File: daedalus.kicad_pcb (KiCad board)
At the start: 4 copper layers, 42 x 50.2 mm, 100 parts, among them J1 CAN Bus, J2 CAN Bus, J5 A Terminal, J6 B Terminal, J7 C Terminal, J9 USB_B_Micro, Q1 AO3401A, U1 XT30, U10 TPH, U11 TPH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

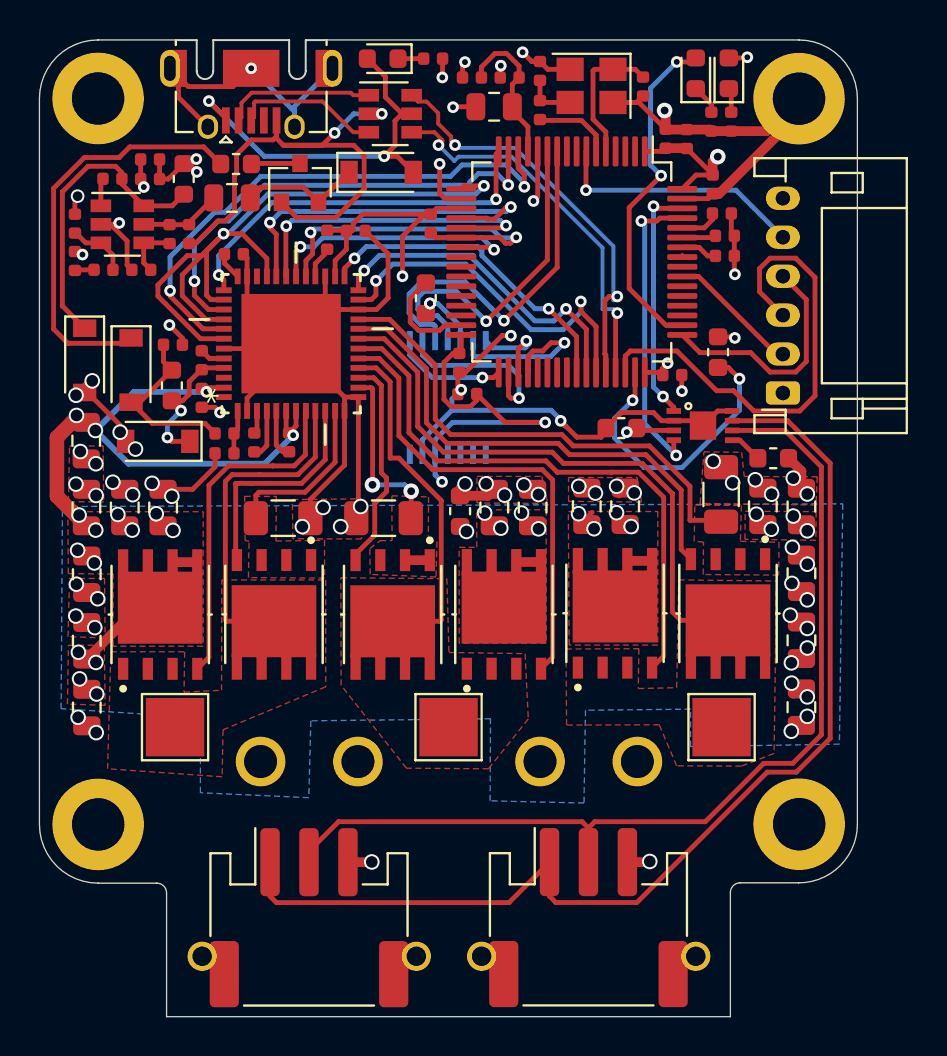
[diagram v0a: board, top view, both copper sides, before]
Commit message: Fixed design rules, fixed pours
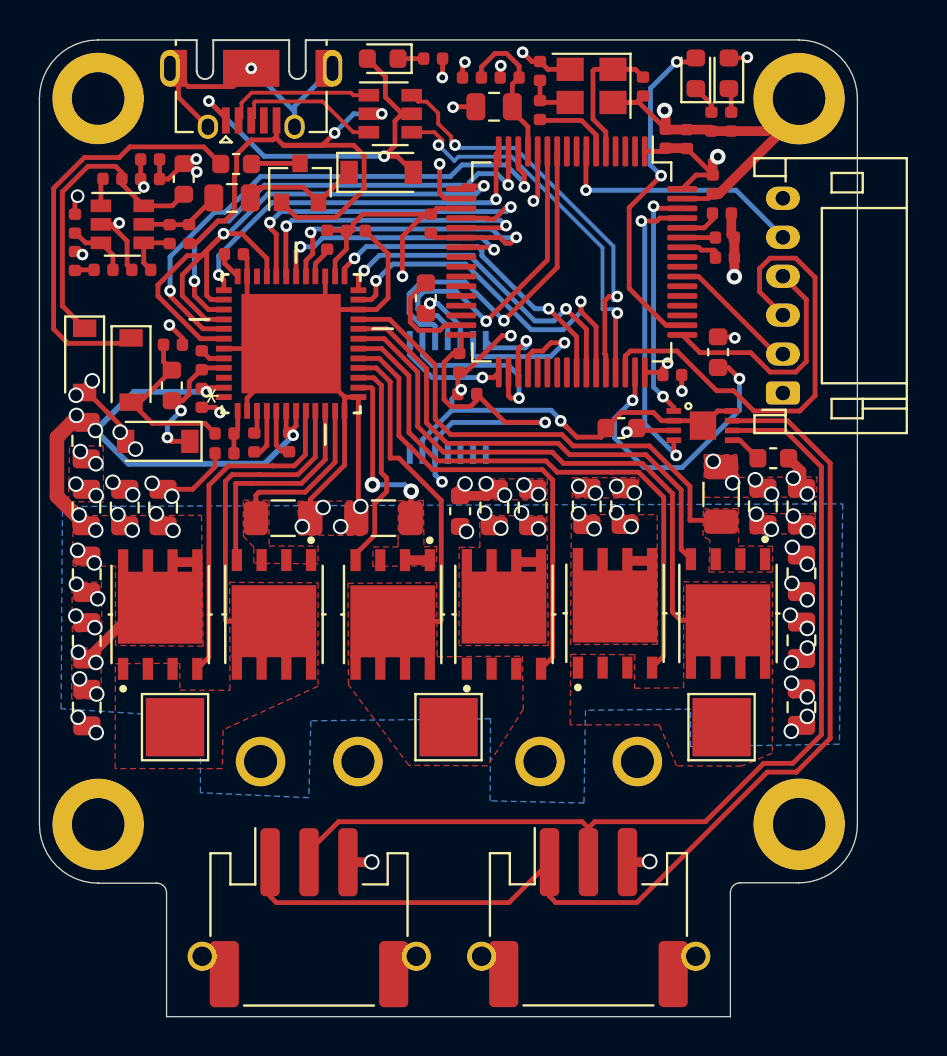
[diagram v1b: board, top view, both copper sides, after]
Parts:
- moved R8 0.09 mm to (158.1, 86.6)
- moved R9 0.09 mm to (158.1, 85.6)
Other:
- net class Default: clearance 0.2 -> 0.16
- rule trace_clearance: 0.2 -> 0.16
- rule trace_min: 0.2 -> 0.16
